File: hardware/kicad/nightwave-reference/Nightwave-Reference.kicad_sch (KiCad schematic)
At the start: 0 parts

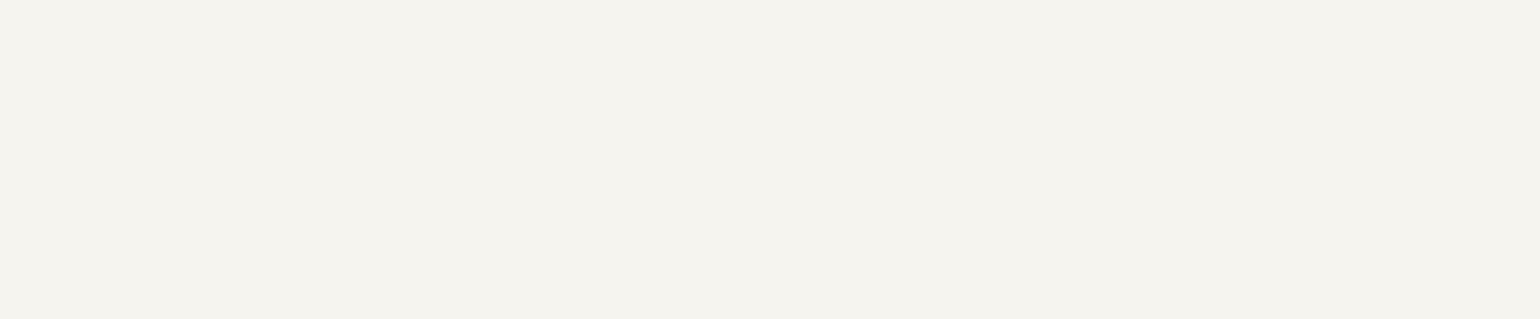
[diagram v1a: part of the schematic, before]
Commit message: Integrate reference board inputs and TFT with typed electrical checks
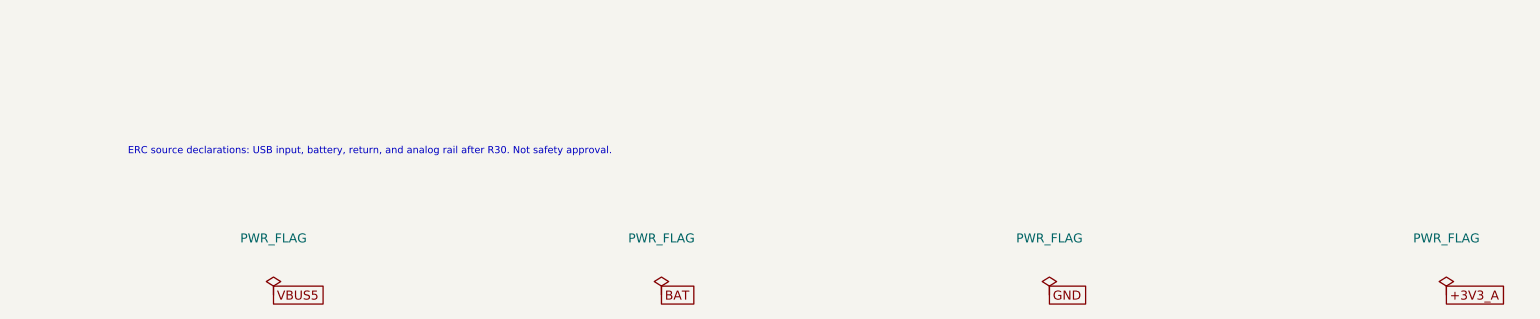
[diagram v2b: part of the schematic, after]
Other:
- note added: "ERC source declarations: USB input, battery, return, and analog rail after R30. Not safety approval."
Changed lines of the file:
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@@
           (property "Sheetfile" "06_connectors_test.kicad_sch" (at 35 220 0) (effects (font (size 1.27 1.27)) (justify left top)))
           (instances (project "Nightwave-Reference" (path "/5aeecf6f-4d30-5388-b813-a754d1969eee" (page "7")))))
+      (text "ERC source declarations: USB input, battery, return, and analog rail after R30. Not safety approval."
+        (at 170 230 0) (effects (font (size 1 1)) (justify left)))
+      (symbol (lib_id "power:PWR_FLAG") (at 190.5 250.19 0) (unit 1)
+          (in_bom no) (on_board yes) (dnp no)
+          (property "Reference" "#FLG0001" (at 190.5 246.19 0) (effects (font (size 1.27 1.27)) (hide yes)))
+          (property "Value" "PWR_FLAG" (at 190.5 242.19 0) (effects (font (size 1.27 1.27))))
+          (pin "1")
+          (instances (project "Nightwave-Reference" (path "/5aeecf6f-4d30-5388-b813-a754d1969eee" (reference "#FLG0001") (unit 1)))))
+          (global_label "VBUS5" (shape passive) (at 190.5 250.19 0)
+            (effects (font (size 1.27 1.27)) (justify left))) (symbol (lib_id "power:PWR_FLAG") (at 245.11 250.19 0) (unit 1)
+          (in_bom no) (on_board yes) (dnp no)
+          (property "Reference" "#FLG0002" (at 245.11 246.19 0) (effects (font (size 1.27 1.27)) (hide yes)))
+          (property "Value" "PWR_FLAG" (at 245.11 242.19 0) (effects (font (size 1.27 1.27))))
+          (pin "1")
+          (instances (project "Nightwave-Reference" (path "/5aeecf6f-4d30-5388-b813-a754d1969eee" (reference "#FLG0002") (unit 1)))))
+          (global_label "BAT" (shape passive) (at 245.11 250.19 0)
+            (effects (font (size 1.27 1.27)) (justify left))) (symbol (lib_id "power:PWR_FLAG") (at 299.72 250.19 0) (unit 1)
+          (in_bom no) (on_board yes) (dnp no)
+          (property "Reference" "#FLG0003" (at 299.72 246.19 0) (effects (font (size 1.27 1.27)) (hide yes)))
+          (property "Value" "PWR_FLAG" (at 299.72 242.19 0) (effects (font (size 1.27 1.27))))
+          (pin "1")
+          (instances (project "Nightwave-Reference" (path "/5aeecf6f-4d30-5388-b813-a754d1969eee" (reference "#FLG0003") (unit 1)))))
+          (global_label "GND" (shape passive) (at 299.72 250.19 0)
+            (effects (font (size 1.27 1.27)) (justify left))) (symbol (lib_id "power:PWR_FLAG") (at 355.6 250.19 0) (unit 1)
+          (in_bom no) (on_board yes) (dnp no)
+          (property "Reference" "#FLG0004" (at 355.6 246.19 0) (effects (font (size 1.27 1.27)) (hide yes)))
+          (property "Value" "PWR_FLAG" (at 355.6 242.19 0) (effects (font (size 1.27 1.27))))
+          (pin "1")
+          (instances (project "Nightwave-Reference" (path "/5aeecf6f-4d30-5388-b813-a754d1969eee" (reference "#FLG0004") (unit 1)))))
+          (global_label "+3V3_A" (shape passive) (at 355.6 250.19 0)
+            (effects (font (size 1.27 1.27)) (justify left)))
       (sheet_instances (path "/" (page "1"))) (embedded_fonts no))
